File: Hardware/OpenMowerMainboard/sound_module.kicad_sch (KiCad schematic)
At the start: 1 part, among them U13 WTV020

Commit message: routing mostly done
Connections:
- net SPEAKER+ renamed SPEAKER_PLUS
- net SPEAKER- renamed SPEAKER_MINUS
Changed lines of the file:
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@@
     (stroke (width 0) (type default) (color 0 0 0 0))
   )
-  (hierarchical_label "SPEAKER-" (shape output) (at 115.57 92.71 180)
+  (hierarchical_label "SPEAKER_MINUS" (shape output) (at 115.57 92.71 180)
     (effects (font (size 1.27 1.27)) (justify right))
   )
@@
     (effects (font (size 1.27 1.27)) (justify right))
   )
-  (hierarchical_label "SPEAKER+" (shape output) (at 115.57 90.17 180)
+  (hierarchical_label "SPEAKER_PLUS" (shape output) (at 115.57 90.17 180)
     (effects (font (size 1.27 1.27)) (justify right))
   )

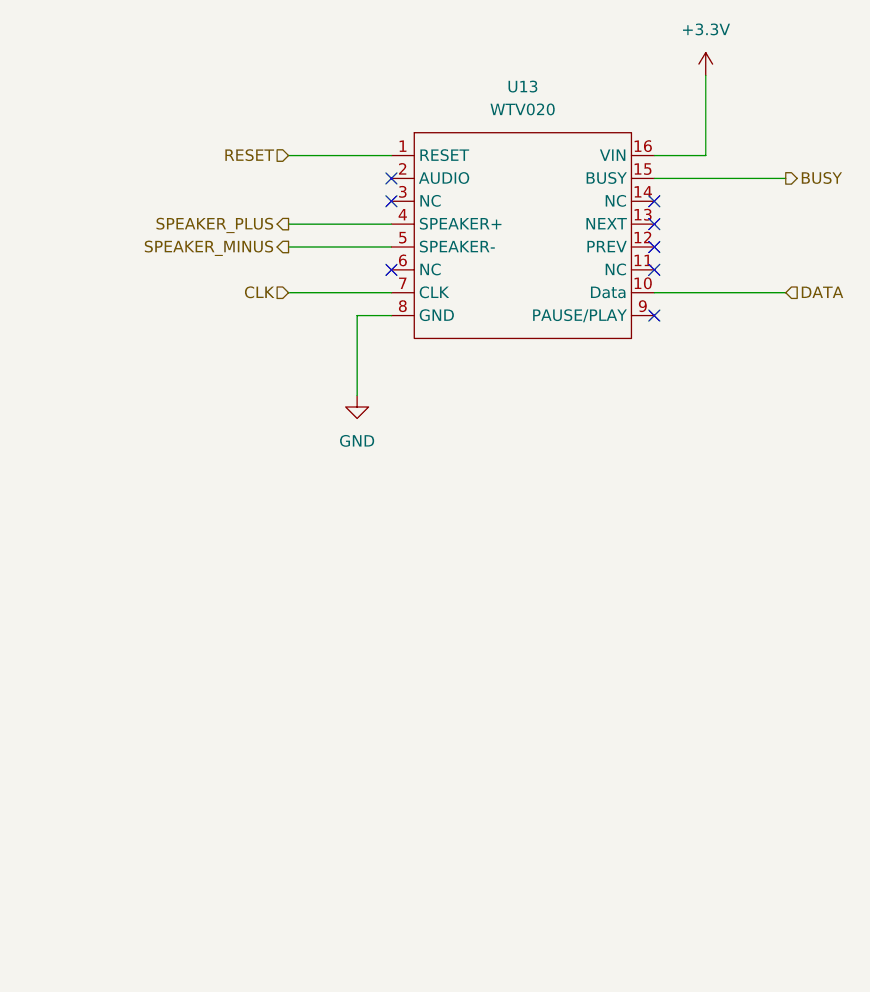
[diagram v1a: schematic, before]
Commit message: v0_9_1 mainboard rework
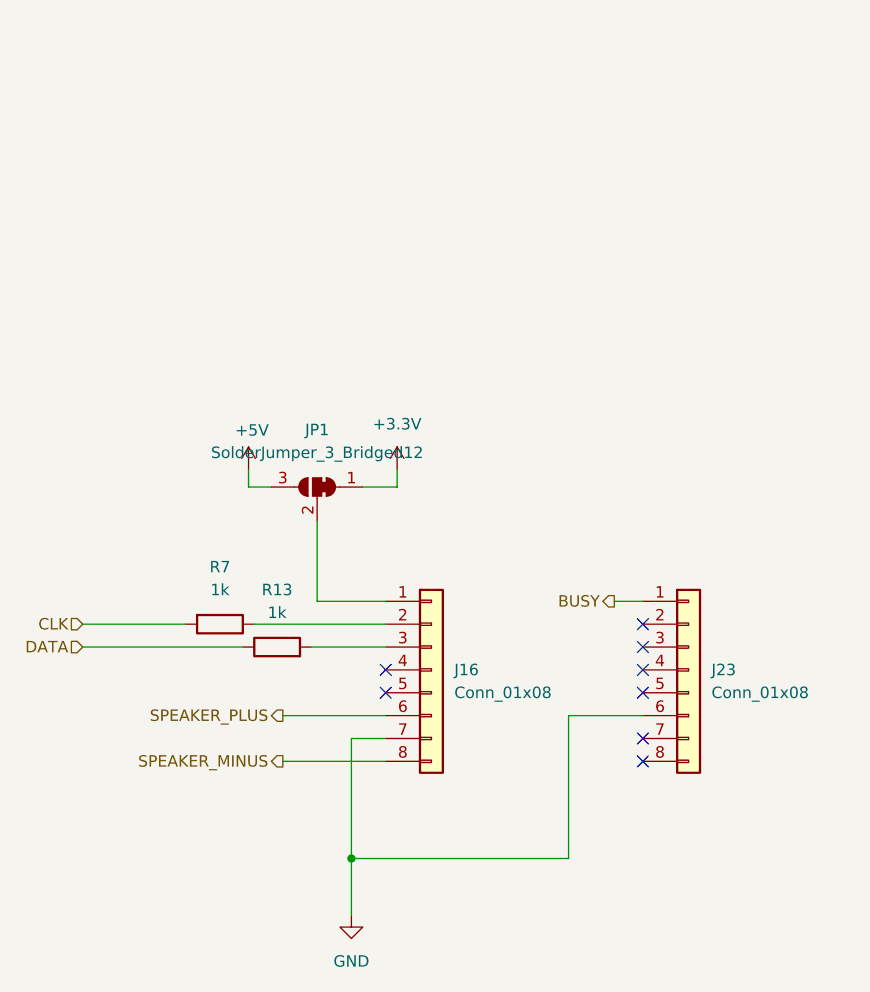
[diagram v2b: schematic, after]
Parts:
- removed U13: WTV020, WTV020:WTV020, symbol OpenMowerMainboardLib:WTV020
- added J16, J23: Conn_01x08, Connector_PinHeader_2.54mm:PinHeader_1x08_P2.54mm_Vertical, symbol Connector_Generic:Conn_01x08
- added JP1: SolderJumper_3_Bridged12, Jumper:SolderJumper-3_P1.3mm_Bridged12_Pad1.0x1.5mm, symbol Jumper:SolderJumper_3_Bridged12
- added R13, R7: 1k, Resistor_SMD:R_0805_2012Metric_Pad1.20x1.40mm_HandSolder, symbol Device:R
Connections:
- net +3V3: now also JP1.1 (A)
- net BUSY: now also J23.1 (Pin_1)
- net CLK: now also R7.2
- net DATA: now also R13.1
- net GND: now also J16.7 (Pin_7), J23.6 (Pin_6)
- net SPEAKER_MINUS: now also J16.8 (Pin_8)
- net SPEAKER_PLUS: now also J16.6 (Pin_6)
- new net: J16.2 (Pin_2), R7.1
- new net: J16.3 (Pin_3), R13.2
- new net: J16.1 (Pin_1), JP1.2 (C)
- new net +5V: JP1.3 (B)

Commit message: BoM data added to kicad - results exported to .xlsx file
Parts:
- J16, J23: LCSC (none) -> C2935914; Part Number (none) -> DZ254R-11-08-63; Stock_PN (none) -> J-TH-1x8-.1
- JP1: Config (none) -> do not place
- R13, R7: Digikey (none) -> 311-1.00KCRCT-ND; Part Number (none) -> RC0805FR-071KL; Stock_PN (none) -> R-805-1K-.125W-1%
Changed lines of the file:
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@@
+      (effects (font (size 1.27 1.27)) hide)
+    )
+    (property "Stock_PN" "R-805-1K-.125W-1%" (id 4) (at 107.95 134.62 0)
+      (effects (font (size 1.27 1.27)) hide)
+    )
+    (property "Digikey" "311-1.00KCRCT-ND" (id 5) (at 107.95 134.62 0)
+      (effects (font (size 1.27 1.27)) hide)
+    )
+    (property "Part Number" "RC0805FR-071KL" (id 6) (at 107.95 134.62 0)
       (effects (font (size 1.27 1.27)) hide)
     )
@@
     )
     (property "Datasheet" "~" (id 3) (at 114.3 137.16 0)
+      (effects (font (size 1.27 1.27)) hide)
+    )
+    (property "Stock_PN" "R-805-1K-.125W-1%" (id 4) (at 114.3 137.16 0)
+      (effects (font (size 1.27 1.27)) hide)
+    )
+    (property "Digikey" "311-1.00KCRCT-ND" (id 5) (at 114.3 137.16 0)
+      (effects (font (size 1.27 1.27)) hide)
+    )
+    (property "Part Number" "RC0805FR-071KL" (id 6) (at 114.3 137.16 0)
       (effects (font (size 1.27 1.27)) hide)
     )
@@
     )
     (property "Datasheet" "~" (id 3) (at 160.02 139.7 0)
+      (effects (font (size 1.27 1.27)) hide)
+    )
+    (property "LCSC" "C2935914" (id 4) (at 160.02 139.7 0)
+      (effects (font (size 1.27 1.27)) hide)
+    )
+    (property "Part Number" "DZ254R-11-08-63" (id 5) (at 160.02 139.7 0)
+      (effects (font (size 1.27 1.27)) hide)
+    )
+    (property "Stock_PN" "J-TH-1x8-.1" (id 6) (at 160.02 139.7 0)
       (effects (font (size 1.27 1.27)) hide)
     )
@@
       (effects (font (size 1.27 1.27)) hide)
     )
+    (property "Config" "do not place" (id 4) (at 118.745 119.38 0)
+      (effects (font (size 1.27 1.27)) hide)
+    )
     (pin "1")
     (pin "2")
@@
       (effects (font (size 1.27 1.27)) hide)
     )
+    (property "LCSC" "C2935914" (id 4) (at 131.445 139.7 0)
+      (effects (font (size 1.27 1.27)) hide)
+    )
+    (property "Part Number" "DZ254R-11-08-63" (id 5) (at 131.445 139.7 0)
+      (effects (font (size 1.27 1.27)) hide)
+    )
+    (property "Stock_PN" "J-TH-1x8-.1" (id 6) (at 131.445 139.7 0)
+      (effects (font (size 1.27 1.27)) hide)
+    )

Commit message: BOM changes
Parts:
- JP1: DNP (none) -> Y
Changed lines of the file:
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@@
+      (effects (font (size 1.27 1.27)) hide)
+    )
+    (property "DNP" "Y" (id 5) (at 118.745 119.38 0)
       (effects (font (size 1.27 1.27)) hide)
     )

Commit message: fix(soundmodule): female socket instead of male headers
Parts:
- J16, J23: footprint Connector_PinHeader_2.54mm:PinHeader_1x08_P2.54mm_Vertical -> Connector_PinSocket_2.54mm:PinSocket_1x08_P2.54mm_Vertical
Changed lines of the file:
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@@
       (effects (font (size 1.27 1.27)) (justify left))
     )
-    (property "Footprint" "Connector_PinHeader_2.54mm:PinHeader_1x08_P2.54mm_Vertical" (id 2) (at 160.02 139.7 0)
+    (property "Footprint" "Connector_PinSocket_2.54mm:PinSocket_1x08_P2.54mm_Vertical" (id 2) (at 160.02 139.7 0)
       (effects (font (size 1.27 1.27)) hide)
     )
@@
       (effects (font (size 1.27 1.27)) (justify left))
     )
-    (property "Footprint" "Connector_PinHeader_2.54mm:PinHeader_1x08_P2.54mm_Vertical" (id 2) (at 131.445 139.7 0)
+    (property "Footprint" "Connector_PinSocket_2.54mm:PinSocket_1x08_P2.54mm_Vertical" (id 2) (at 131.445 139.7 0)
       (effects (font (size 1.27 1.27)) hide)
     )

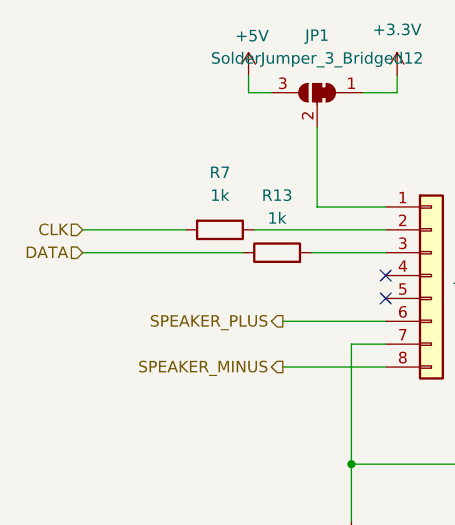
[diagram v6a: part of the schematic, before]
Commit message: fix(imu): update and reroute sound/imu connections
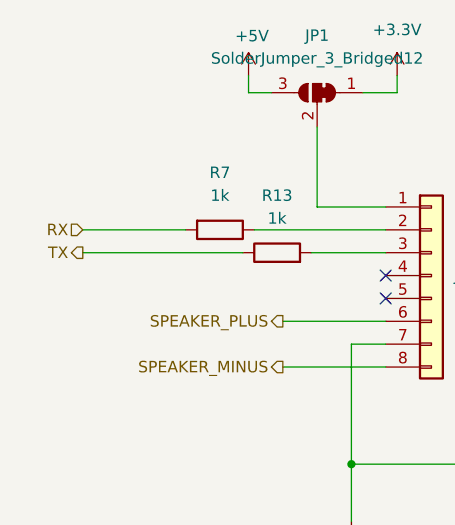
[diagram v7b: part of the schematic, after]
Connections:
- net CLK renamed RX
- net DATA renamed TX
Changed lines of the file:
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@@
     (effects (font (size 1.27 1.27)) (justify right))
   )
-  (hierarchical_label "DATA" (shape input) (at 92.71 137.16 180)
+  (hierarchical_label "TX" (shape output) (at 92.71 137.16 180)
     (effects (font (size 1.27 1.27)) (justify right))
   )
-  (hierarchical_label "CLK" (shape input) (at 92.71 134.62 180)
+  (hierarchical_label "RX" (shape input) (at 92.71 134.62 180)
     (effects (font (size 1.27 1.27)) (justify right))
   )

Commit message: feat(sound): deprecate DFplayer (R7,R13,J17,J23)
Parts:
- J16, J23: Config (none) -> do not place; now left out of the parts list
- R13, R7: Config (none) -> no not place; now left out of the parts list
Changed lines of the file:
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@@
   )
   (symbol (lib_id "Device:R") (at 107.95 134.62 270) (unit 1)
-    (in_bom yes) (on_board yes) (fields_autoplaced)
+    (in_bom no) (on_board yes) (fields_autoplaced)
     (property "Reference" "R7" (id 0) (at 107.95 128.27 90))
     (property "Value" "1k" (id 1) (at 107.95 130.81 90))
@@
       (effects (font (size 1.27 1.27)) hide)
     )
+    (property "Config" "no not place" (id 7) (at 107.95 134.62 0)
+      (effects (font (size 1.27 1.27)) hide)
+    )
     (pin "1")
     (pin "2")
   )
   (symbol (lib_id "Device:R") (at 114.3 137.16 90) (unit 1)
-    (in_bom yes) (on_board yes) (fields_autoplaced)
+    (in_bom no) (on_board yes) (fields_autoplaced)
     (property "Reference" "R13" (id 0) (at 114.3 130.81 90))
     (property "Value" "1k" (id 1) (at 114.3 133.35 90))
@@
       (effects (font (size 1.27 1.27)) hide)
     )
+    (property "Config" "no not place" (id 7) (at 114.3 137.16 0)
+      (effects (font (size 1.27 1.27)) hide)
+    )
     (pin "1")
     (pin "2")
   )
   (symbol (lib_id "Connector_Generic:Conn_01x08") (at 160.02 139.7 0) (unit 1)
-    (in_bom yes) (on_board yes) (fields_autoplaced)
+    (in_bom no) (on_board yes) (fields_autoplaced)
     (property "Reference" "J23" (id 0) (at 162.56 139.6999 0)
       (effects (font (size 1.27 1.27)) (justify left))
@@
     )
     (property "Stock_PN" "J-TH-1x8-.1" (id 6) (at 160.02 139.7 0)
+      (effects (font (size 1.27 1.27)) hide)
+    )
+    (property "Config" "do not place" (id 7) (at 160.02 139.7 0)
       (effects (font (size 1.27 1.27)) hide)
     )
@@
   )
   (symbol (lib_id "Connector_Generic:Conn_01x08") (at 131.445 139.7 0) (unit 1)
-    (in_bom yes) (on_board yes) (fields_autoplaced)
+    (in_bom no) (on_board yes) (fields_autoplaced)
     (property "Reference" "J16" (id 0) (at 133.985 139.6999 0)
       (effects (font (size 1.27 1.27)) (justify left))
@@
       (effects (font (size 1.27 1.27)) hide)
     )
+    (property "Config" "do not place" (id 7) (at 131.445 139.7 0)
+      (effects (font (size 1.27 1.27)) hide)
+    )
